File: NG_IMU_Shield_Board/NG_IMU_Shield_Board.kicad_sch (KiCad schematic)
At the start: 22 parts, among them J1 Conn_01x04_Female, J2 Conn_01x02_Male, J3 Conn_01x10_Female, J4 Conn_01x03_Female, J5 Conn_02x12_Top_Bottom, J6 Conn_01x11_Male, U1 SN75ALS175, U2 Level_Converter, U3 Teensy_v4.0

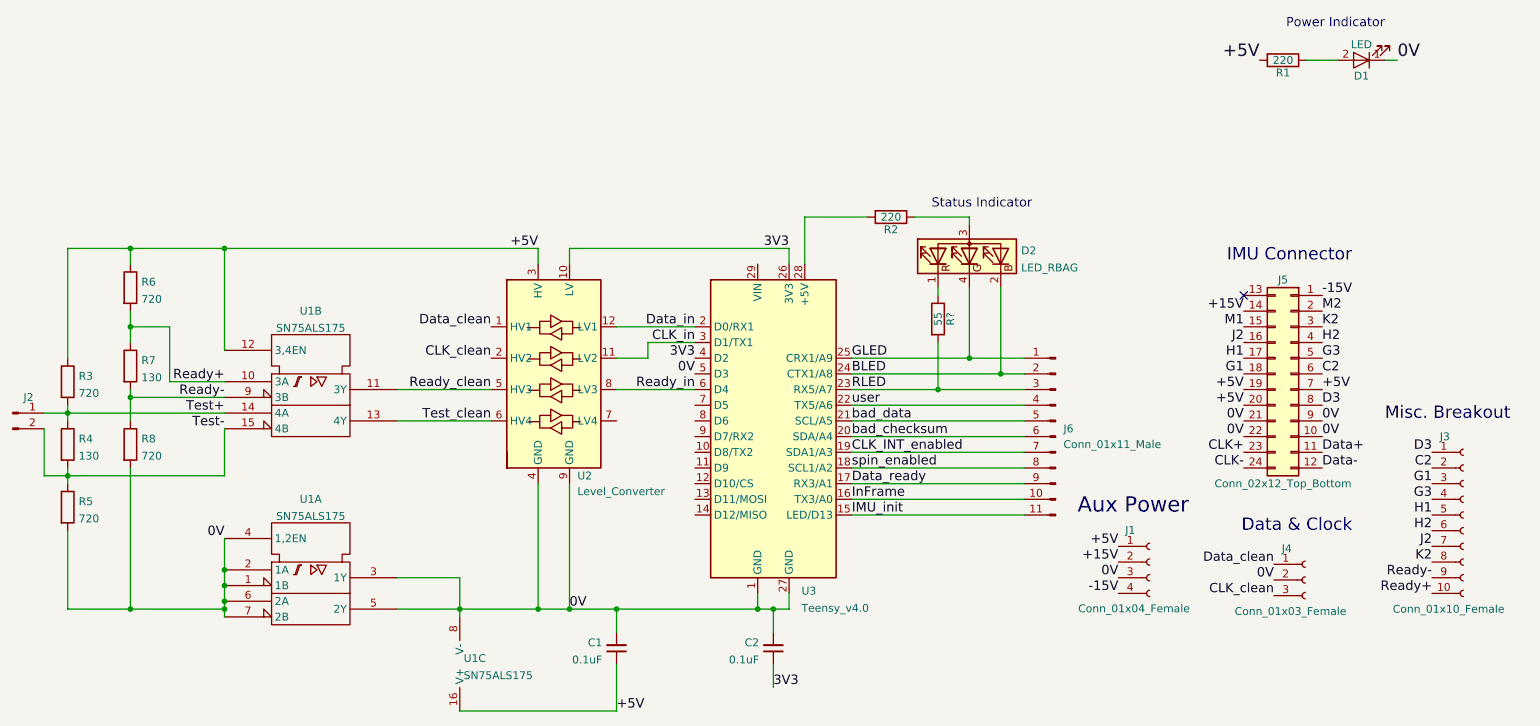
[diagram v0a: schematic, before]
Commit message: Changed to use LM393 and completed schematic
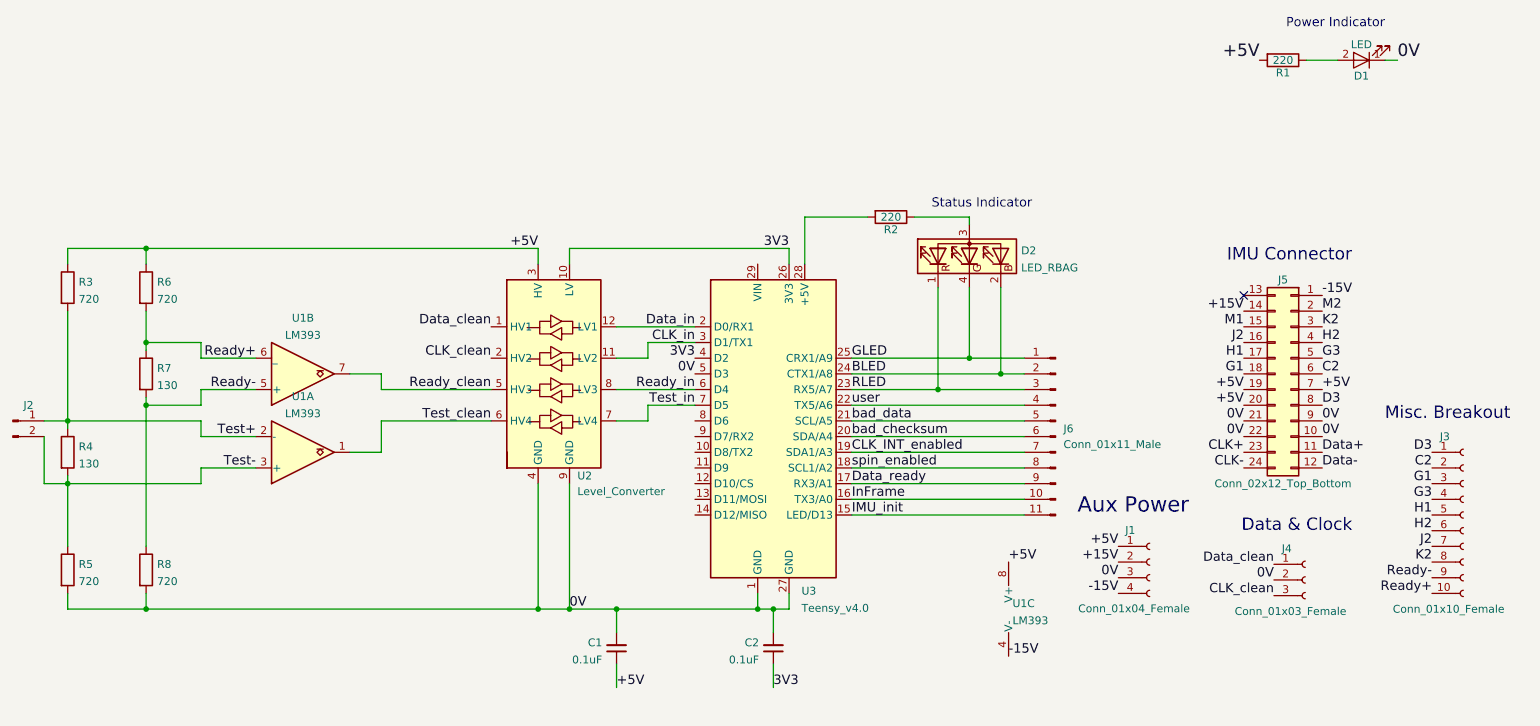
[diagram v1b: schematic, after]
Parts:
- removed R?: 55, Resistor_THT:R_Axial_DIN0204_L3.6mm_D1.6mm_P7.62mm_Horizontal, symbol NG_IMU_Interface_Board-rescue:R
- removed U1: SN75ALS175, Package_DIP:DIP-16_W7.62mm_Socket, symbol NG_IMU_Shield_Board:SN75ALS175
- added U1: LM393, Package_DIP:DIP-8_W7.62mm, symbol Comparator:LM393
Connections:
- net +5V: now also U1.8 (V+)
- net -15V: now also U1.4 (V-)
- net RLED: now also D2.1 (RK)
- net Ready+: now also U1.6 (_)
- net Ready-: now also U1.5 (+)
- net Ready_clean: now also U1.7
- net Test+: now also U1.2 (-)
- net Test-: now also U1.3 (+)
- net Test_clean: now also U1.1
- net Test_in: now reaches U3.7 (D5)
- net Test_in: now also U2.7 (LV4)
